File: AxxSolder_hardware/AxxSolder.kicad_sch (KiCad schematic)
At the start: 156 parts, among them IC1 TLV76733DRVR, IC2 OPA2387DSGT, IC3 LMR54406DBVR, IC4 STM32G431CBT6, IC5 TPD4E1U06DBVR, IC6 STUSB4500QTR, IC7 MAX16171ATA_VY+T, IC8 LTC4440AHMS8E, IC9 INA281A5QDBVRQ1, J1 USB4110-GF-A, J2 691243110009, J3 TSW-102-07-T-S, J4 61300611821, J5 TSW-102-07-T-S, J6 TSW-102-07-T-S, J7 TSW-108-07-T-S, J8 Conn_01x01_Pin, Q1 STL9P3LLH6, Q2 STL10N3LLH5, Q3 2N7002NXAKR, U2 PEC11J-9215F-S0015, U3 BSC014N04LS

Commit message: enlarged board
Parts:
- added J9: TSW-102-07-T-S, footprints:TSW-102-XX-YY-S, symbol TSW-102-07-T-S:TSW-102-07-T-S
- J8: footprint (none) -> footprints:TSW-102-XX-YY-S
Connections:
- net +7.5V: now also J9.1 (Pin_1)
- net GND: now also J9.2 (Pin_2)
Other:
- moved on the sheet: H3, H4, H5, H6
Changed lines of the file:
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@@
 	)
 	(junction
+		(at 26.67 189.23)
+		(diameter 0)
+		(color 0 0 0 0)
+	)
+	(junction
+		(at 17.78 187.96)
+		(diameter 0)
+		(color 0 0 0 0)
+	)
+	(junction
 		(at 22.86 163.195)
 		(diameter 0)
@@
 	(wire
 		(pts
+			(xy 24.13 189.23) (xy 26.67 189.23)
+		)
+		(stroke
+			(width 0)
+			(type default)
+		)
+	)
+	(wire
+		(pts
 			(xy 16.51 163.195) (xy 22.86 163.195)
 		)
@@
 		)
 	)
+	(wire
+		(pts
+			(xy 17.78 189.23) (xy 17.78 187.96)
+		)
+		(stroke
+			(width 0)
+			(type default)
+		)
+	)
 	(polyline
 		(pts
@@
 	(wire
 		(pts
+			(xy 21.59 189.23) (xy 17.78 189.23)
+		)
+		(stroke
+			(width 0)
+			(type default)
+		)
+	)
+	(wire
+		(pts
 			(xy 135.89 186.69) (xy 135.89 187.96)
 		)
@@
 	)
 	(symbol
+		(lib_name "TSW-102-07-T-S_1")
+		(lib_id "TSW-102-07-T-S:TSW-102-07-T-S")
+		(at 24.13 189.23 90)
+		(unit 1)
+		(exclude_from_sim no)
+		(in_bom yes)
+		(on_board yes)
+		(dnp no)
+		(property "Reference" "J9"
+			(at 23.114 187.198 0)
+			(effects
+				(font
+					(size 1.27 1.27)
+				)
+			)
+		)
+		(property "Value" "TSW-102-07-T-S"
+			(at 18.796 193.675 0)
+			(effects
+				(font
+					(size 1.27 1.27)
+				)
+				(hide yes)
+			)
+		)
+		(property "Footprint" "footprints:TSW-102-XX-YY-S"
+			(at 119.05 172.72 0)
+			(effects
+				(font
+					(size 1.27 1.27)
+				)
+				(justify left top)
+				(hide yes)
+			)
+		)
+		(property "Datasheet" "http://suddendocs.samtec.com/prints/tsw-xxx-xx-xxx-x-xx-xxx-mkt.pdf"
+			(at 219.05 172.72 0)
+			(effects
+				(font
+					(size 1.27 1.27)
+				)
+				(justify left top)
+				(hide yes)
+			)
+		)
+		(property "Description" ""
+			(at 24.13 189.23 0)
+			(effects
+				(font
+					(size 1.27 1.27)
+				)
+			)
+		)
+		(property "Height" ""
+			(at 419.05 172.72 0)
+			(effects
+				(font
+					(size 1.27 1.27)
+				)
+				(justify left top)
+				(hide yes)
+			)
+		)
+		(property "Mouser Part Number" "200-TSW10207TS"
+			(at 519.05 172.72 0)
+			(effects
+				(font
+					(size 1.27 1.27)
+				)
+				(justify left top)
+				(hide yes)
+			)
+		)
+		(property "Mouser Price/Stock" "https://www.mouser.co.uk/ProductDetail/Samtec/TSW-102-07-T-S?qs=hzq9O0YpnZuE%252BS9CaLPVlQ%3D%3D"
+			(at 619.05 172.72 0)
+			(effects
+				(font
+					(size 1.27 1.27)
+				)
+				(justify left top)
+				(hide yes)
+			)
+		)
+		(property "Manufacturer_Name" "SAMTEC"
+			(at 719.05 172.72 0)
+			(effects
+				(font
+					(size 1.27 1.27)
+				)
+				(justify left top)
+				(hide yes)
+			)
+		)
+		(property "Manufacturer_Part_Number" "TSW-102-07-T-S"
+			(at 819.05 172.72 0)
+			(effects
+				(font
+					(size 1.27 1.27)
+				)
+				(justify left top)
+				(hide yes)
+			)
+		)
+		(property "Manufacturing comment" "Do Not Place"
+			(at 24.13 189.23 0)
+			(effects
+				(font
+					(size 1.27 1.27)
+				)
+				(hide yes)
+			)
+		)
+		(pin "1"
+		)
+		(pin "2"
+		)
+		(instances
+			(project "AxxSolder"
+				(path "/d71363c3-4d90-469c-a600-831e2a7cdaef"
+					(reference "J9")
+					(unit 1)
+				)
+			)
+		)
+	)
+	(symbol
 		(lib_id "Device:R_Small")
 		(at 219.964 150.876 270)
@@
 		(lib_name "MountingHole_3")
 		(lib_id "Mechanical:MountingHole")
-		(at 54.61 191.77 0)
+		(at 62.23 189.23 0)
 		(unit 1)
 		(exclude_from_sim yes)
@@
 		(fields_autoplaced yes)
 		(property "Reference" "H5"
-			(at 57.15 190.4999 0)
+			(at 64.77 187.9599 0)
 			(effects
 				(font
@@
 		)
 		(property "Value" "MountingHole"
-			(at 57.15 193.0399 0)
+			(at 64.77 190.4999 0)
 			(effects
 				(font
@@
 		)
 		(property "Footprint" "MountingHole:MountingHole_3.2mm_M3"
-			(at 54.61 191.77 0)
+			(at 62.23 189.23 0)
 			(effects
 				(font
@@
 		)
 		(property "Datasheet" "~"
-			(at 54.61 191.77 0)
+			(at 62.23 189.23 0)
 			(effects
 				(font
@@
 		)
 		(property "Description" "Mounting Hole without connection"
-			(at 54.61 191.77 0)
+			(at 62.23 189.23 0)
 			(effects
 				(font
@@
 		(lib_name "MountingHole_4")
 		(lib_id "Mechanical:MountingHole")
-		(at 62.23 191.77 0)
+		(at 69.85 189.23 0)
 		(unit 1)
 		(exclude_from_sim yes)
@@
 		(fields_autoplaced yes)
 		(property "Reference" "H6"
-			(at 64.77 190.4999 0)
+			(at 72.39 187.9599 0)
 			(effects
 				(font
@@
 		)
 		(property "Value" "MountingHole"
-			(at 64.77 193.0399 0)
+			(at 72.39 190.4999 0)
 			(effects
 				(font
@@
 		)
 		(property "Footprint" "MountingHole:MountingHole_3.2mm_M3"
-			(at 62.23 191.77 0)
+			(at 69.85 189.23 0)
 			(effects
 				(font
@@
 		)
 		(property "Datasheet" "~"
-			(at 62.23 191.77 0)
+			(at 69.85 189.23 0)
 			(effects
 				(font
@@
 		)
 		(property "Description" "Mounting Hole without connection"
-			(at 62.23 191.77 0)
+			(at 69.85 189.23 0)
 			(effects
 				(font
@@
 		(lib_name "MountingHole_2")
 		(lib_id "Mechanical:MountingHole")
-		(at 45.72 191.77 0)
+		(at 53.34 189.23 0)
 		(unit 1)
 		(exclude_from_sim yes)
@@
 		(fields_autoplaced yes)
 		(property "Reference" "H4"
-			(at 48.26 190.4999 0)
+			(at 55.88 187.9599 0)
 			(effects
 				(font
@@
 		)
 		(property "Value" "MountingHole"
-			(at 48.26 193.0399 0)
+			(at 55.88 190.4999 0)
 			(effects
 				(font
@@
 		)
 		(property "Footprint" "MountingHole:MountingHole_3.2mm_M3"
-			(at 45.72 191.77 0)
+			(at 53.34 189.23 0)
 			(effects
 				(font
@@
 		)
 		(property "Datasheet" "~"
-			(at 45.72 191.77 0)
+			(at 53.34 189.23 0)
 			(effects
 				(font
@@
 		)
 		(property "Description" "Mounting Hole without connection"
-			(at 45.72 191.77 0)
+			(at 53.34 189.23 0)
 			(effects
 				(font
@@
 			)
 		)
-		(property "Footprint" ""
+		(property "Footprint" "footprints:TSW-102-XX-YY-S"
 			(at 143.383 103.632 0)
 			(effects
@@
 		(lib_name "MountingHole_1")
 		(lib_id "Mechanical:MountingHole")
-		(at 38.1 191.77 0)
+		(at 45.72 189.23 0)
 		(unit 1)
 		(exclude_from_sim yes)
@@
 		(fields_autoplaced yes)
 		(property "Reference" "H3"
-			(at 40.64 190.4999 0)
+			(at 48.26 187.9599 0)
 			(effects
 				(font
@@
 		)
 		(property "Value" "MountingHole"
-			(at 40.64 193.0399 0)
+			(at 48.26 190.4999 0)
 			(effects
 				(font
@@
 		)
 		(property "Footprint" "MountingHole:MountingHole_3.2mm_M3"
-			(at 38.1 191.77 0)
+			(at 45.72 189.23 0)
 			(effects
 				(font
@@
 		)
 		(property "Datasheet" "~"
-			(at 38.1 191.77 0)
+			(at 45.72 189.23 0)
 			(effects
 				(font
@@
 		)
 		(property "Description" "Mounting Hole without connection"
-			(at 38.1 191.77 0)
+			(at 45.72 189.23 0)
 			(effects
 				(font

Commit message: updated layout
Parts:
- J8: footprint footprints:TSW-102-XX-YY-S -> footprints:TSW-101-XX-YY-S
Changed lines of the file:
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@@
 			)
 		)
-		(property "Footprint" "footprints:TSW-102-XX-YY-S"
+		(property "Footprint" "footprints:TSW-101-XX-YY-S"
 			(at 143.383 103.632 0)
 			(effects

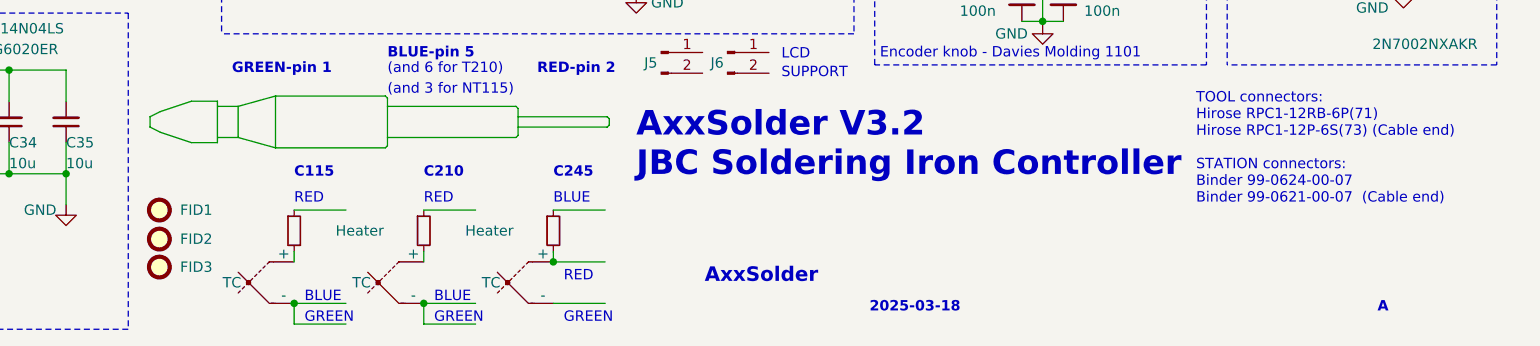
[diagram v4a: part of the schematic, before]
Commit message: deleted fuducials
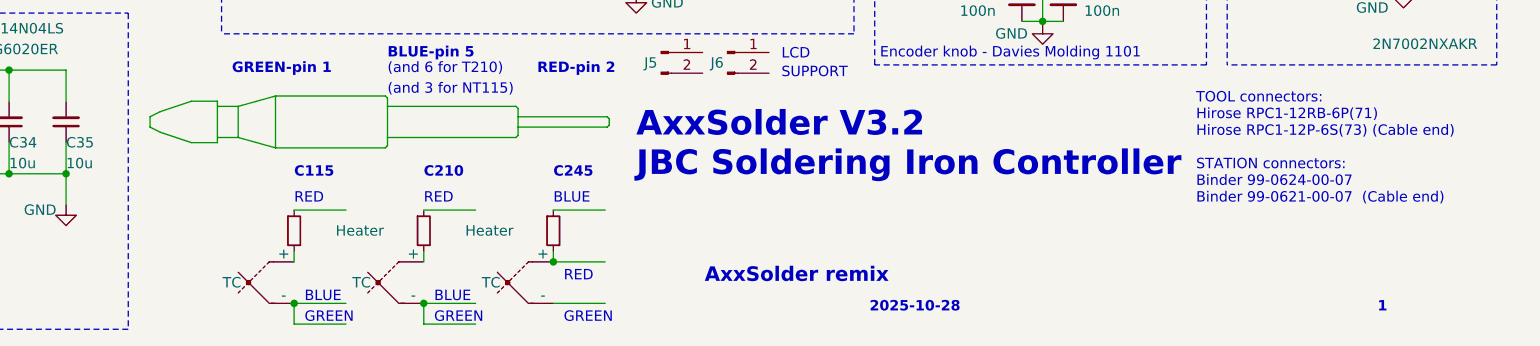
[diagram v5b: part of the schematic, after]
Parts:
- removed FID1, FID2, FID3: Fiducial, Fiducial:Fiducial_0.75mm_Mask1.5mm, symbol Mechanical:Fiducial
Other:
- note added: "1"
- note added: "2025-10-28"
- note added: "AxxSolder remix"
- note removed: "2025-03-18"
- note removed: "A"
- note removed: "AxxSolder"
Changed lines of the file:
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@@
 		)
 	)
-	(text "A"
+	(text "1"
 		(exclude_from_sim no)
 		(at 268.605 194.31 0)
@@
 		)
 	)
-	(text "2025-03-18"
+	(text "2025-10-28"
 		(exclude_from_sim no)
 		(at 206.375 194.31 0)
@@
 		)
 	)
-	(text "AxxSolder"
+	(text "AxxSolder remix"
 		(exclude_from_sim no)
 		(at 186.182 190.754 0)
@@
 	)
 	(symbol
-		(lib_id "Mechanical:Fiducial")
-		(at 119.38 188.595 0)
-		(unit 1)
-		(exclude_from_sim no)
-		(in_bom no)
-		(on_board yes)
-		(dnp no)
-		(property "Reference" "FID3"
-			(at 121.92 188.595 0)
-			(effects
-				(font
-					(size 1.27 1.27)
-				)
-				(justify left)
-			)
-		)
-		(property "Value" "Fiducial"
-			(at 121.92 189.865 0)
-			(effects
-				(font
-					(size 1.27 1.27)
-				)
-				(justify left)
-				(hide yes)
-			)
-		)
-		(property "Footprint" "Fiducial:Fiducial_0.75mm_Mask1.5mm"
-			(at 119.38 188.595 0)
-			(effects
-				(font
-					(size 1.27 1.27)
-				)
-				(hide yes)
-			)
-		)
-		(property "Datasheet" "~"
-			(at 119.38 188.595 0)
-			(effects
-				(font
-					(size 1.27 1.27)
-				)
-				(hide yes)
-			)
-		)
-		(property "Description" ""
-			(at 119.38 188.595 0)
-			(effects
-				(font
-					(size 1.27 1.27)
-				)
-			)
-		)
-		(property "Manufacturing comment" "Do Not Place"
-			(at 119.38 188.595 0)
-			(effects
-				(font
-					(size 1.27 1.27)
-				)
-				(hide yes)
-			)
-		)
-		(instances
-			(project "AxxSolder"
-				(path "/d71363c3-4d90-469c-a600-831e2a7cdaef"
-					(reference "FID3")
-					(unit 1)
-				)
-			)
-		)
-	)
-	(symbol
 		(lib_id "power:GND")
 		(at 194.31 29.21 0)
@@
 	)
 	(symbol
-		(lib_id "Mechanical:Fiducial")
-		(at 119.38 185.166 0)
-		(unit 1)
-		(exclude_from_sim no)
-		(in_bom no)
-		(on_board yes)
-		(dnp no)
-		(property "Reference" "FID2"
-			(at 121.92 185.166 0)
-			(effects
-				(font
-					(size 1.27 1.27)
-				)
-				(justify left)
-			)
-		)
-		(property "Value" "Fiducial"
-			(at 121.92 186.436 0)
-			(effects
-				(font
-					(size 1.27 1.27)
-				)
-				(justify left)
-				(hide yes)
-			)
-		)
-		(property "Footprint" "Fiducial:Fiducial_0.75mm_Mask1.5mm"
-			(at 119.38 185.166 0)
-			(effects
-				(font
-					(size 1.27 1.27)
-				)
-				(hide yes)
-			)
-		)
-		(property "Datasheet" "~"
-			(at 119.38 185.166 0)
-			(effects
-				(font
-					(size 1.27 1.27)
-				)
-				(hide yes)
-			)
-		)
-		(property "Description" ""
-			(at 119.38 185.166 0)
-			(effects
-				(font
-					(size 1.27 1.27)
-				)
-			)
-		)
-		(property "Manufacturing comment" "Do Not Place"
-			(at 119.38 185.166 0)
-			(effects
-				(font
-					(size 1.27 1.27)
-				)
-				(hide yes)
-			)
-		)
-		(instances
-			(project "AxxSolder"
-				(path "/d71363c3-4d90-469c-a600-831e2a7cdaef"
-					(reference "FID2")
-					(unit 1)
-				)
-			)
-		)
-	)
-	(symbol
 		(lib_id "Device:R_Small")
 		(at 76.2 83.312 180)
@@
 					(unit 1)
 				)
-			)
-		)
-	)
-	(symbol
-		(lib_id "Mechanical:Fiducial")
-		(at 119.38 181.61 0)
-		(unit 1)
-		(exclude_from_sim no)
-		(in_bom no)
-		(on_board yes)
-		(dnp no)
-		(property "Reference" "FID1"
-			(at 121.92 181.61 0)
-			(effects
-				(font
-					(size 1.27 1.27)
-				)
-				(justify left)
-			)
-		)
-		(property "Value" "Fiducial"
-			(at 121.92 182.88 0)
-			(effects
-				(font
-					(size 1.27 1.27)
-				)
-				(justify left)
-				(hide yes)
-			)
-		)
-		(property "Footprint" "Fiducial:Fiducial_0.75mm_Mask1.5mm"
-			(at 119.38 181.61 0)
-			(effects
-				(font
-					(size 1.27 1.27)
-				)
-				(hide yes)
-			)
-		)
-		(property "Datasheet" "~"
-			(at 119.38 181.61 0)
-			(effects
-				(font
-					(size 1.27 1.27)
-				)
-				(hide yes)
-			)
-		)
-		(property "Description" ""
-			(at 119.38 181.61 0)
-			(effects
-				(font
-					(size 1.27 1.27)
-				)
-			)
-		)
-		(property "Manufacturing comment" "Do Not Place"
-			(at 119.38 181.61 0)
-			(effects
-				(font
-					(size 1.27 1.27)
-				)
-				(hide yes)
-			)
-		)
-		(instances
-			(project "AxxSolder"
-				(path "/d71363c3-4d90-469c-a600-831e2a7cdaef"
-					(reference "FID1")
-					(unit 1)
-				)
